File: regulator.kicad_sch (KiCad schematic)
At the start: 28 parts, among them U4 TPS63020DSJR, U5 MD53R33

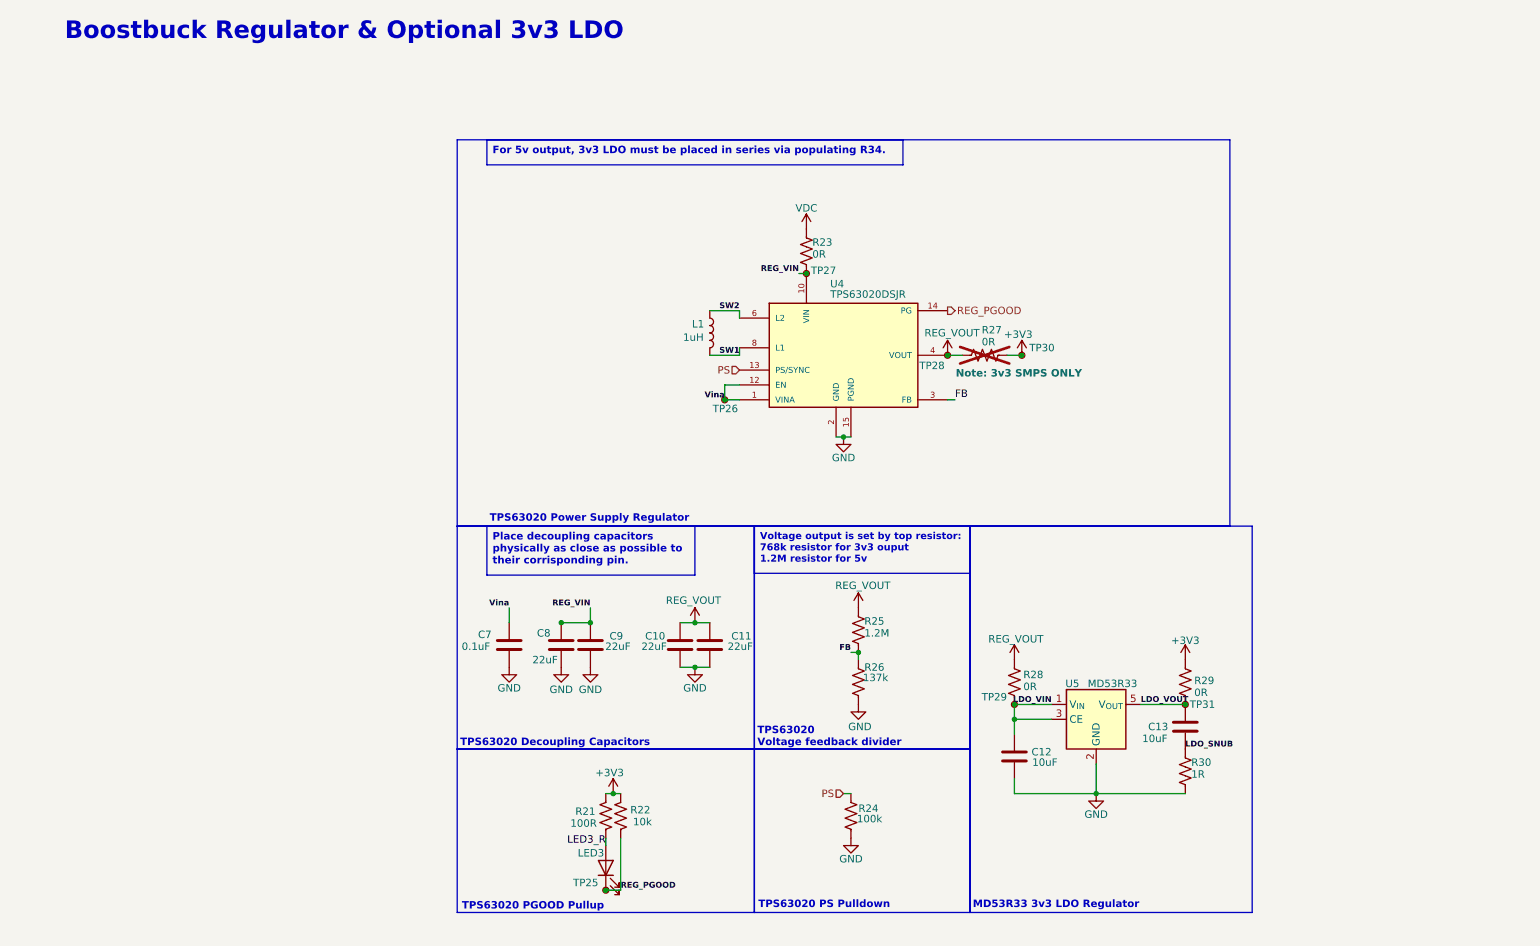
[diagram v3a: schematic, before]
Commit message: Started work on PCB layout
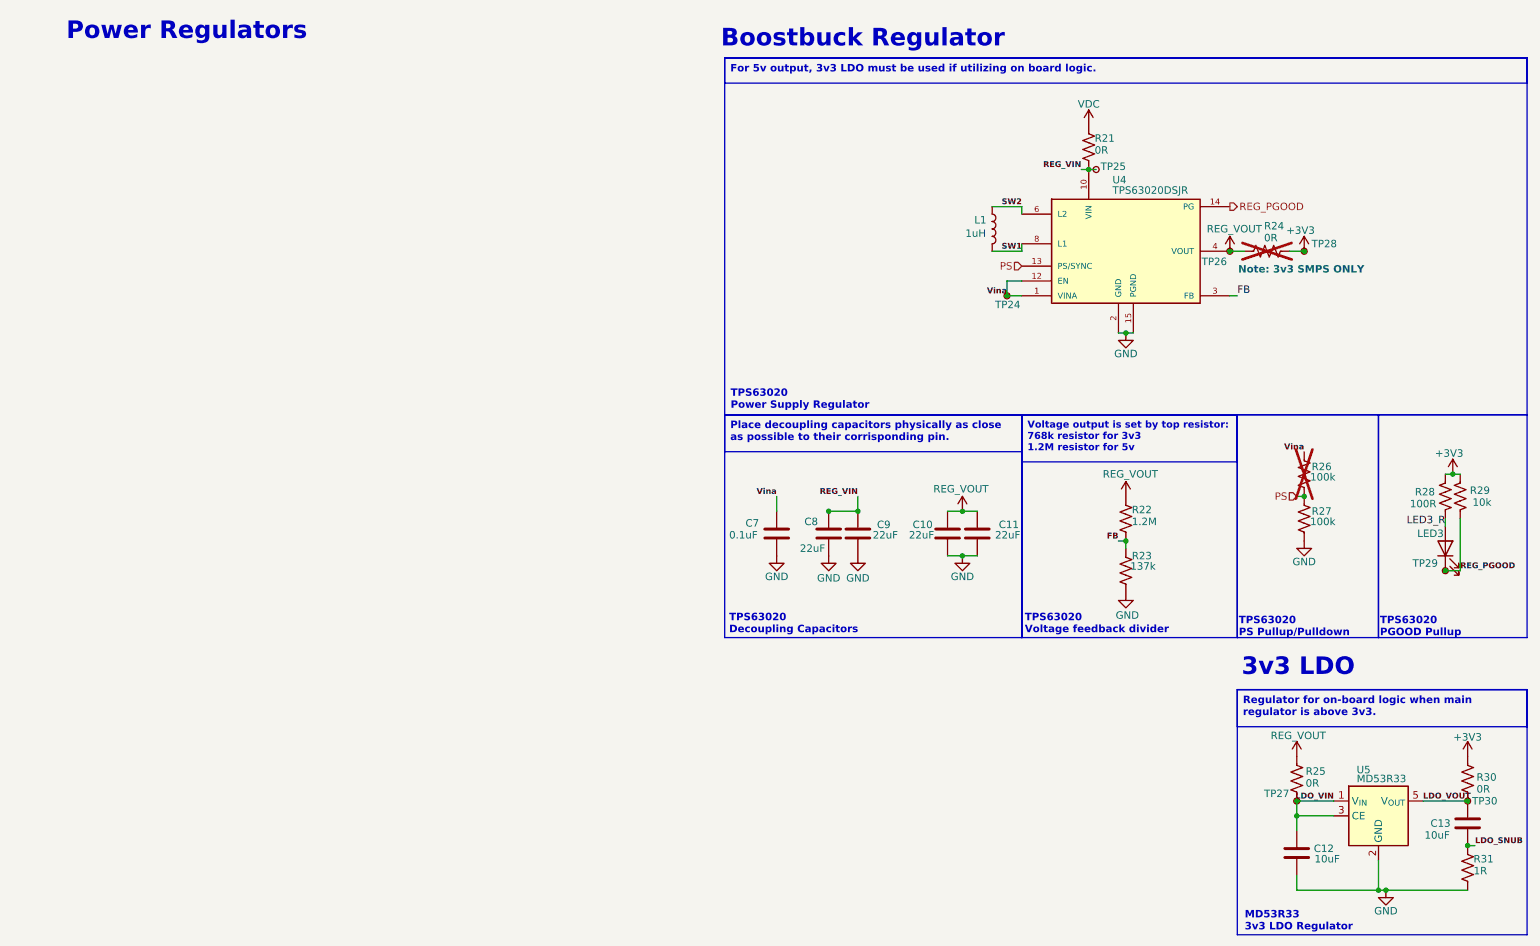
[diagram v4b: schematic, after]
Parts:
- added R26: 100k, Resistor_SMD:R_0603_1608Metric, symbol Device:R_US
- TP24: renamed from TP26; footprint (none) -> TestPoint:TestPoint_Pad_D1.0mm
- TP25: renamed from TP27; footprint (none) -> TestPoint:TestPoint_Pad_D1.0mm
- TP27: renamed from TP29; footprint (none) -> TestPoint:TestPoint_Pad_D1.0mm
- TP29: renamed from TP25; footprint (none) -> TestPoint:TestPoint_Pad_D1.0mm
- TP30: renamed from TP31; footprint (none) -> TestPoint:TestPoint_Pad_D1.0mm
- renumbered R23 to R21, R25 to R22, R26 to R23, R27 to R24, R28 to R25, R24 to R27, R21 to R28, R22 to R29, R29 to R30, R30 to R31, TP28 to TP26, TP30 to TP28
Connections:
- net PS: now also R26.2
- net Vina: now also R26.1
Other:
- note added: "3v3 LDO"
- note added: "Boostbuck Regulator"
- note added: "Power Regulators"
- note added: "TPS63020 PS Pullup/Pulldown"
- note removed: "Boostbuck Regulator & Optional 3v3 LDO"
- note removed: "TPS63020 PS Pulldown"
- moved on the sheet: C10, C11, C12, C13, C7, C8, C9, L1, LED3, R21, R22, R23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

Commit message: Initial commit
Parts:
- removed TP29: REG_PGOOD, TestPoint:TestPoint_Pad_D1.0mm, symbol Connector:TestPoint_Small
- added NT1: NetTie_2, NetTie:NetTie-2_SMD_Pad2.0mm, symbol Device:NetTie_2
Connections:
- net REG_VIN: now also NT1.2
- net Vina: no longer U4.1 (VINA), U4.12 (EN)
- new net REG_EN: NT1.1, U4.12 (EN)
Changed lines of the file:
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@@
-	)
-	(junction
-		(at 248.92 109.22)
-		(diameter 0)
-		(color 0 0 0 0)
 	)
 	(junction
@@
 	)
 	(junction
-		(at 173.99 62.23)
-		(diameter 0)
-		(color 0 0 0 0)
-	)
-	(junction
 		(at 250.19 92.71)
 		(diameter 0)
@@
 	(wire
 		(pts
-			(xy 251.46 109.22) (xy 248.92 109.22)
-		)
-		(stroke
-			(width 0)
-			(type default)
-		)
-	)
-	(wire
-		(pts
 			(xy 213.36 62.23) (xy 212.09 62.23)
 		)
@@
 	(wire
 		(pts
+			(xy 166.37 40.64) (xy 166.37 49.53)
+		)
+		(stroke
+			(width 0)
+			(type default)
+		)
+	)
+	(wire
+		(pts
 			(xy 248.92 92.71) (xy 250.19 92.71)
 		)
@@
 	(wire
 		(pts
+			(xy 248.92 109.22) (xy 251.46 109.22)
+		)
+		(stroke
+			(width 0)
+			(type default)
+		)
+	)
+	(wire
+		(pts
 			(xy 134.62 96.52) (xy 134.62 99.06)
 		)
@@
 	(wire
 		(pts
-			(xy 173.99 62.23) (xy 176.53 62.23)
+			(xy 173.99 62.23) (xy 171.45 62.23)
 		)
 		(stroke
@@
 	(wire
 		(pts
+			(xy 166.37 40.64) (xy 187.96 40.64)
+		)
+		(stroke
+			(width 0)
+			(type default)
+		)
+	)
+	(wire
+		(pts
 			(xy 166.37 106.68) (xy 168.91 106.68)
 		)
@@
 	(wire
 		(pts
-			(xy 186.69 40.64) (xy 187.96 40.64)
-		)
-		(stroke
-			(width 0)
-			(type default)
-		)
-	)
-	(wire
-		(pts
 			(xy 223.52 161.29) (xy 223.52 163.83)
 		)
@@
 	(wire
 		(pts
+			(xy 176.53 59.69) (xy 166.37 59.69)
+		)
+		(stroke
+			(width 0)
+			(type default)
+		)
+	)
+	(wire
+		(pts
 			(xy 223.52 151.13) (xy 223.52 153.67)
 		)
@@
 	(wire
 		(pts
+			(xy 166.37 54.61) (xy 166.37 59.69)
+		)
+		(stroke
+			(width 0)
+			(type default)
+		)
+	)
+	(wire
+		(pts
 			(xy 193.04 104.14) (xy 194.31 104.14)
 		)
@@
 	(wire
 		(pts
-			(xy 173.99 59.69) (xy 176.53 59.69)
-		)
-		(stroke
-			(width 0)
-			(type default)
-		)
-	)
-	(wire
-		(pts
 			(xy 238.76 163.83) (xy 252.73 163.83)
 		)
@@
 		(pts
 			(xy 250.19 92.71) (xy 251.46 92.71)
-		)
-		(stroke
-			(width 0)
-			(type default)
-		)
-	)
-	(wire
-		(pts
-			(xy 173.99 59.69) (xy 173.99 62.23)
 		)
 		(stroke
@@
 	)
 	(label "Vina"
-		(at 173.99 62.23 180)
+		(at 173.99 62.23 0)
 		(effects
 			(font
@@
 				(bold yes)
 			)
-			(justify right bottom)
+			(justify left bottom)
 		)
 	)
@@
 				(thickness 0.2)
 				(bold yes)
+			)
+			(justify right bottom)
+		)
+	)
+	(label "REG_EN"
+		(at 176.53 59.69 180)
+		(effects
+			(font
+				(size 1.27 1.27)
 			)
 			(justify right bottom)
@@
 		)
 		(instances
-			(project "regulator"
-				(path "/020756ea-5278-4889-90aa-85efc1608834"
-					(reference "LED2")
-					(unit 1)
-				)
-			)
 			(project "power_module"
 				(path "/33e2b92e-f705-4be7-96f4-57092b8ec1ea/8030bb5b-b463-45e7-87db-4ab635727d1f"
@@
 	)
 	(symbol
-		(lib_id "Connector:TestPoint_Small")
-		(at 248.92 109.22 0)
-		(mirror y)
+		(lib_id "Device:NetTie_2")
+		(at 166.37 52.07 90)
 		(unit 1)
 		(body_style 1)
 		(exclude_from_sim no)
-		(in_bom yes)
+		(in_bom no)
 		(on_board yes)
 		(in_pos_files yes)
 		(dnp no)
-		(property "Reference" "TP29"
-			(at 247.65 107.9499 0)
+		(property "Reference" "NT1"
+			(at 165.1 50.7999 90)
 			(show_name no)
 			(do_not_autoplace no)
@@
 			)
 		)
-		(property "Value" "REG_PGOOD"
-			(at 247.65 110.4899 0)
-			(hide yes)
+		(property "Value" "NetTie_2"
+			(at 165.1 53.3399 90)
 			(show_name no)
 			(do_not_autoplace no)
@@
 			)
 		)
-		(property "Footprint" "TestPoint:TestPoint_Pad_D1.0mm"
-			(at 243.84 109.22 0)
+		(property "Footprint" "NetTie:NetTie-2_SMD_Pad2.0mm"
+			(at 166.37 52.07 0)
 			(hide yes)
 			(show_name no)
@@
 		)
 		(property "Datasheet" ""
-			(at 243.84 109.22 0)
-			(hide yes)
-			(show_name no)
-			(do_not_autoplace no)
-			(effects
-				(font
-					(size 1.27 1.27)
-				)
-			)
-		)
-		(property "Description" "test point"
-			(at 248.92 109.22 0)
-			(hide yes)
-			(show_name no)
-			(do_not_autoplace no)
-			(effects
-				(font
-					(size 1.27 1.27)
-				)
-			)
+			(at 166.37 52.07 0)
+			(hide yes)
+			(show_name no)
+			(do_not_autoplace no)
+			(effects
+				(font
+					(size 1.27 1.27)
+				)
+			)
+		)
+		(property "Description" "Net tie, 2 pins"
+			(at 166.37 52.07 0)
+			(hide yes)
+			(show_name no)
+			(do_not_autoplace no)
+			(effects
+				(font
+					(size 1.27 1.27)
+				)
+			)
+		)
+		(pin "2"
 		)
 		(pin "1"
@@
 			(project "power_module"
 				(path "/33e2b92e-f705-4be7-96f4-57092b8ec1ea/8030bb5b-b463-45e7-87db-4ab635727d1f"
-					(reference "TP29")
-					(unit 1)
-				)
+					(reference "NT1")
+					(unit 1)
+				)
